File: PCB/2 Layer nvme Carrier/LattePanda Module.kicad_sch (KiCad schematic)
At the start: 23 parts, among them J1 Conn_01x03_Pin, J81 Conn_01x02_Pin, U80 W25Q128JVSIQ

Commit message: Parts change for BOM
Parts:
- A1: Mfr.# (none) -> ADDR0069-P009A
- BT1: Mfr.# (none) -> S8411-45R
- C86: Mfr.# (none) -> CL05A226MQ5QUNC
- C87: Mfr.# (none) -> 0402B104K160CT
- D78: Mfr.# (none) -> RB521C30-2/TR
- J1: Mfr.# (none) -> 2.54-1*3
- J81: Mfr.# (none) -> 2.54-1*2
- R1: Mfr.# (none) -> RC0402FR-071KL
- R2: Mfr.# (none) -> RC0402FR-0710KL
- R76, R77: Mfr.# (none) -> RC0402FR-07100KL
- R80: Mfr.# (none) -> RMC 0402 0R N
- R81, R82, R83, R84, R85: Mfr.# (none) -> RC0402FR-0715RL
- R86: Mfr.# (none) -> RC0402FR-07120KL
- U80: Mfr.# (none) -> W25Q128JVSIQ

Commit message: BOM update and pdf
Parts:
- A1: MPN (none) -> ADDR0069-P009A; Mfr.# ADDR0069-P009A -> (none)
- BT1: MPN (none) -> S8411-45R; Mfr.# S8411-45R -> (none)
- C86: MPN (none) -> CL05A226MQ5QUNC; Mfr.# CL05A226MQ5QUNC -> (none)
- C87: MPN (none) -> 0402B104K160CT; Mfr.# 0402B104K160CT -> (none)
- D78: MPN (none) -> RB521C30-2/TR; Mfr.# RB521C30-2/TR -> (none)
- J1: MPN (none) -> 2.54-1*3; Mfr.# 2.54-1*3 -> (none)
- J81: MPN (none) -> 2.54-1*2; Mfr.# 2.54-1*2 -> (none)
- R1: MPN (none) -> RC0402FR-071KL; Mfr.# RC0402FR-071KL -> (none)
- R2: MPN (none) -> RC0402FR-0710KL; Mfr.# RC0402FR-0710KL -> (none)
- R76, R77: MPN (none) -> RC0402FR-07100KL; Mfr.# RC0402FR-07100KL -> (none)
- R80: MPN (none) -> RMC 0402 0R N; Mfr.# RMC 0402 0R N -> (none)
- R81, R82, R83, R84, R85: MPN (none) -> RC0402FR-0715RL; Mfr.# RC0402FR-0715RL -> (none)
- R86: MPN (none) -> RC0402FR-07120KL; Mfr.# RC0402FR-07120KL -> (none)
- U80: MPN (none) -> W25Q128JVSIQ; Mfr.# W25Q128JVSIQ -> (none)
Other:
- note added: "HSIO functions are defined by the BIOS source code, Cannot be changed in BIOS settings. The functions are defined as follows: - HSIO0: USB3.2 10Gbps - HSIO1: PCIe 3.0 x1 M.2 - HSIO2: PCIe 3.0 x1 M.2 - HSIO3: PCIe 3.0 x1 M.2 - HSIO8: PCIe 3.0 x1 M.2 - HSIO9: PCIe 3.0 x1 M.2 - HSIO10: PCIe 3.0 x1 M.2 - HSIO11: PCIe 3.0 x4 (x1) - HSIO6: PCIe 3.0 x4 (x1)"
- note removed: "HSIO functions are defined by the BIOS source code, Cannot be changed in BIOS settings. The functions are defined as follows: - HSIO0: USB3.2 10Gbps - HSIO1: PCIe 3.0 x1 M.2 - HSIO2: PCIe 3.0 x1 M.2 - HSIO3: PCIe 3.0 x1 M.2 - HSIO8: PCIe 3.0 x1 M.2 - HSIO9: PCIe 3.0 x1 M.2 - HSIO10: PCIe 3.0 x1 M.2 - HSIO11: PCIe 3.0 x4 (Lane 1) - HSIO6: PCIe 3.0 x4 (Lane 1)"

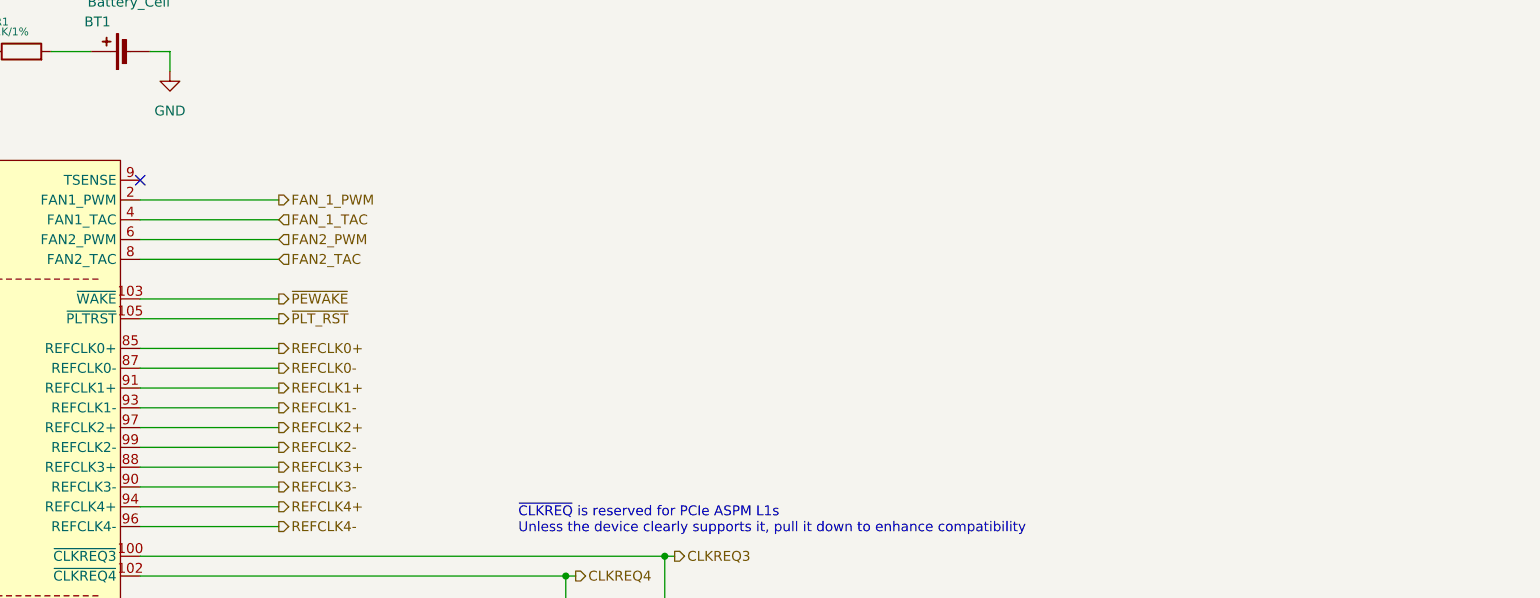
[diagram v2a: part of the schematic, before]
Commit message: Rework for PSU and REFCLK
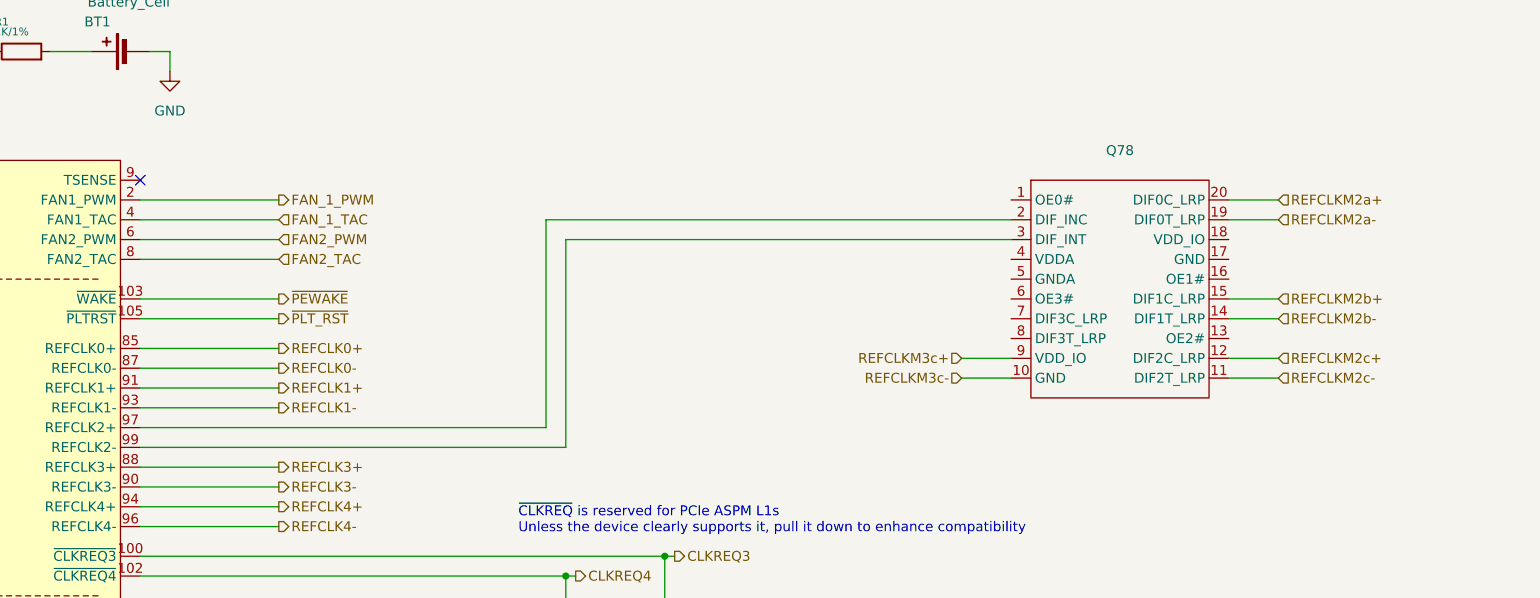
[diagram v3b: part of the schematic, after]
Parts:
- added Q78: ~, Package_SO:TSSOP-20_4.4x6.5mm_P0.65mm, symbol User:9DBL411BGLFT
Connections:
- net REFCLK2+: no longer names the net of A1.97 (REFCLK2+)
- net REFCLK2+: now also Q78.2 (DIF_INC)
- net REFCLK2-: no longer names the net of A1.99 (REFCLK2-)
- net REFCLK2-: now also Q78.3 (DIF_INT)
- new net REFCLKM2a+: Q78.20 (DIF0C_LRP)
- new net REFCLKM2a-: Q78.19 (DIF0T_LRP)
- new net REFCLKM2b+: Q78.15 (DIF1C_LRP)
- new net REFCLKM2b-: Q78.14 (DIF1T_LRP)
- new net REFCLKM2c+: Q78.12 (DIF2C_LRP)
- new net REFCLKM2c-: Q78.11 (DIF2T_LRP)
- new net REFCLKM3c+: Q78.9 (VDD_IO)
- new net REFCLKM3c-: Q78.10 (GND)

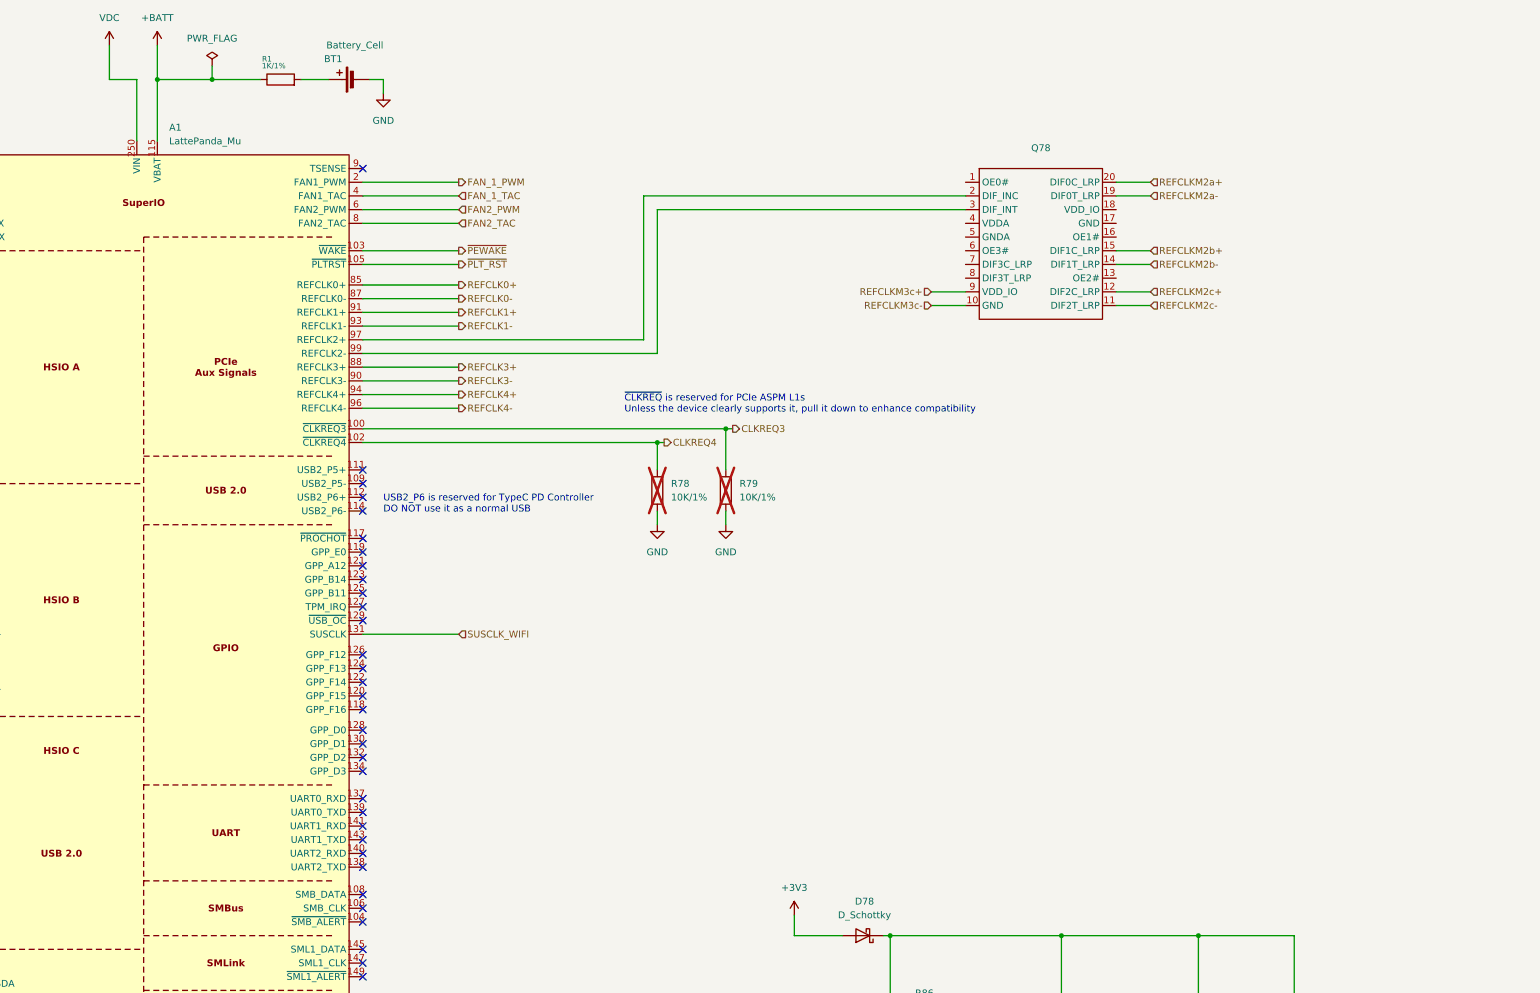
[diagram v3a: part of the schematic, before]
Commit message: change to 12V and more work to do
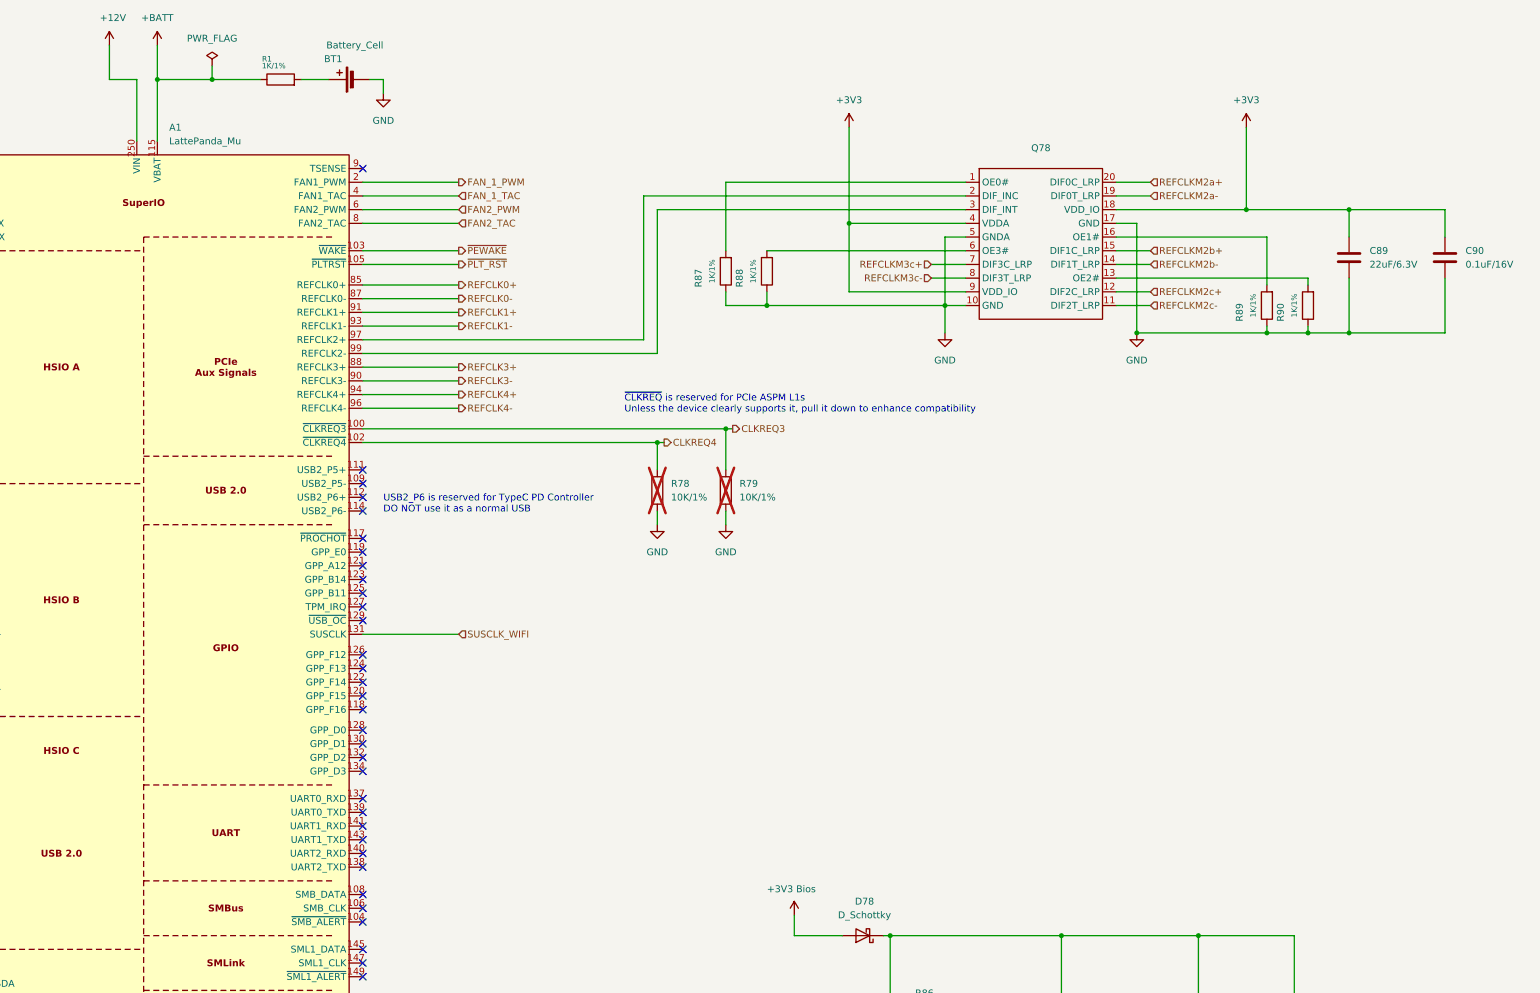
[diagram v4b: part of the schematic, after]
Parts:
- added C89: 22uF/6.3V, A_HDJ_Library:C_0402_1005Metric, symbol Device:C
- added C90: 0.1uF/16V, A_HDJ_Library:C_0402_1005Metric, symbol Device:C
- added R87, R88, R89, R90: 1K/1%, A_HDJ_Library:R_0402_1005Metric, symbol Device:R
- J81: MPN 2.54-1*2 -> PZ2.54-1*2
- Q78: MPN (none) -> 9DBL411BGLFT
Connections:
- net +3V3: now also Q78.18 (VDD_IO), Q78.4 (VDDA), Q78.9 (VDD_IO), C89.1, C90.1; no longer D78.2 (A)
- net GND: now also Q78.10 (GND), Q78.17 (GND), Q78.5 (GNDA), C89.2, C90.2, R87.1, R88.1, R89.1, R90.1
- net REFCLKM3c+: now also Q78.7 (DIF3C_LRP); no longer Q78.9 (VDD_IO)
- net REFCLKM3c-: now also Q78.8 (DIF3T_LRP); no longer Q78.10 (GND)
- net at Q78.1 (OE0#): now also R87.2
- net at Q78.13 (OE2#): now also R90.2
- net at Q78.16 (OE1#): now also R89.2
- net at Q78.6 (OE3#): now also R88.2
- net VDC renamed +12V
- new net +3V3 Bios: D78.2 (A)

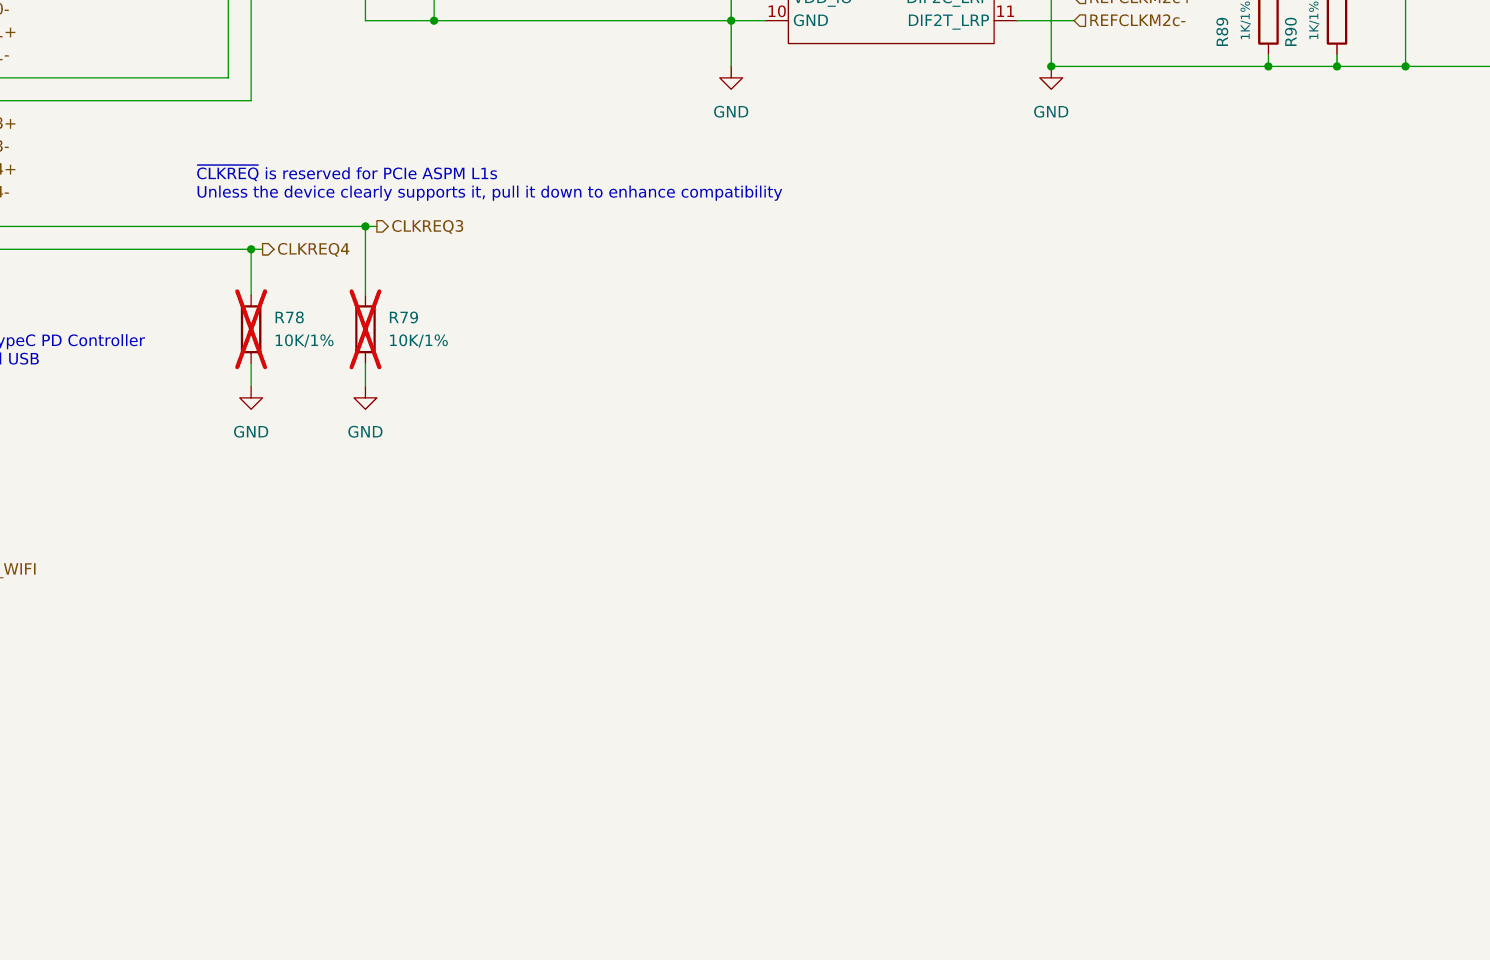
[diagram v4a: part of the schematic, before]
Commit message: Add new Buffer Chip for rework
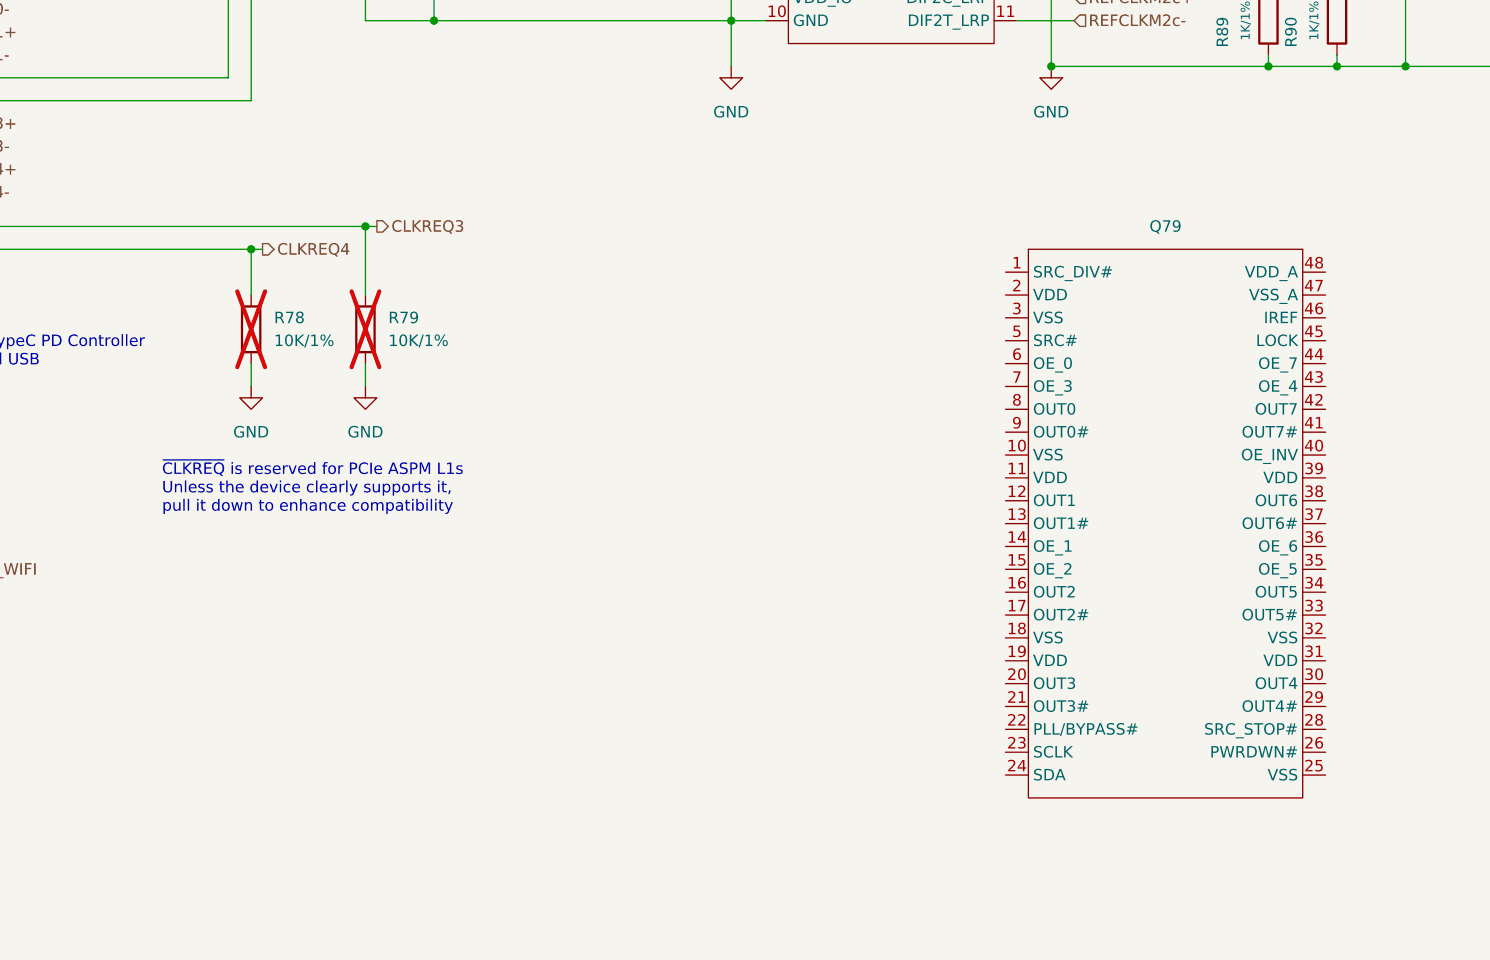
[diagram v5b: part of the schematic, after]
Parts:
- added Q79: ~, Package_SO:TSSOP-48_6.1x12.5mm_P0.5mm, symbol User:PI6C20800AE
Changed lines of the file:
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@@
 		)
 	)
-	(text "~{CLKREQ} is reserved for PCIe ASPM L1s\nUnless the device clearly supports it, pull it down to enhance compatibility"
+	(text "~{CLKREQ} is reserved for PCIe ASPM L1s\nUnless the device clearly supports it,\npull it down to enhance compatibility"
 		(exclude_from_sim no)
-		(at 400.304 104.648 0)
+		(at 396.494 138.43 0)
 		(effects
 			(font
@@
 					(unit 1)
 				)
+			)
+		)
+	)
+	(symbol
+		(lib_id "User:PI6C20800AE")
+		(at 508 142.24 0)
+		(unit 1)
+		(exclude_from_sim no)
+		(in_bom no)
+		(on_board yes)
+		(dnp no)
+		(fields_autoplaced yes)
+		(property "Reference" "Q79"
+			(at 508 109.22 0)
+			(effects
+				(font
+					(size 1.27 1.27)
+				)
+			)
+		)
+		(property "Value" "~"
+			(at 505.46 137.16 0)
+			(effects
+				(font
+					(size 1.27 1.27)
+				)
+				(hide yes)
+			)
+		)
+		(property "Footprint" "Package_SO:TSSOP-48_6.1x12.5mm_P0.5mm"
+			(at 505.46 137.16 0)
+			(effects
+				(font
+					(size 1.27 1.27)
+				)
+				(hide yes)
+			)
+		)
+		(property "Datasheet" "https://www.digikey.ch/htmldatasheets/production/1248881/0/0/1/PI6C20800.pdf"
+			(at 505.46 137.16 0)
+			(effects
+				(font
+					(size 1.27 1.27)
+				)
+				(hide yes)
+			)
+		)
+		(property "Description" ""
+			(at 505.46 137.16 0)
+			(effects
+				(font
+					(size 1.27 1.27)
+				)
+				(hide yes)
+			)
+		)
+		(property "MPN" "PI6C20800AE"
+			(at 508 142.24 0)
+			(effects
+				(font
+					(size 1.27 1.27)
+				)
+				(hide yes)
+			)
+		)
+		(pin "7"
+		)
+		(pin "28"
+		)
+		(pin "26"
+		)
+		(pin "2"
+		)
+		(pin "21"
+		)
+		(pin "12"
+		)
+		(pin "23"
+		)
+		(pin "11"
+		)
+		(pin "16"
+		)
+		(pin "17"
+		)
+		(pin "3"
+		)
+		(pin "45"
+		)
+		(pin "40"
+		)
+		(pin "31"
+		)
+		(pin "47"
+		)
+		(pin "43"
+		)
+		(pin "33"
+		)
+		(pin "22"
+		)
+		(pin "39"
+		)
+		(pin "1"
+		)
+		(pin "14"
+		)
+		(pin "15"
+		)
+		(pin "19"
+		)
+		(pin "35"
+		)
+		(pin "38"
+		)
+		(pin "41"
+		)
+		(pin "42"
+		)
+		(pin "18"
+		)
+		(pin "48"
+		)
+		(pin "5"
+		)
+		(pin "13"
+		)
+		(pin "30"
+		)
+		(pin "8"
+		)
+		(pin "46"
+		)
+		(pin "10"
+		)
+		(pin "20"
+		)
+		(pin "24"
+		)
+		(pin "36"
+		)
+		(pin "32"
+		)
+		(pin "29"
+		)
+		(pin "34"
+		)
+		(pin "37"
+		)
+		(pin "6"
+		)
+		(pin "25"
+		)
+		(pin "44"
+		)
+		(pin "9"
+		)
+		(instances
+			(project "nvme Carrier for LattePanda Mu"
+				(path "/2a6d114a-7fd7-4207-b5f7-4ea9c34f36aa/6eee02c2-78c9-4e83-9ccf-e0f7690b57bf"
+					(reference "Q79")
+					(unit 1)
+				)
